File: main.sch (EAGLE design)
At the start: 50 parts, among them U1 SN65HVD10_D_8

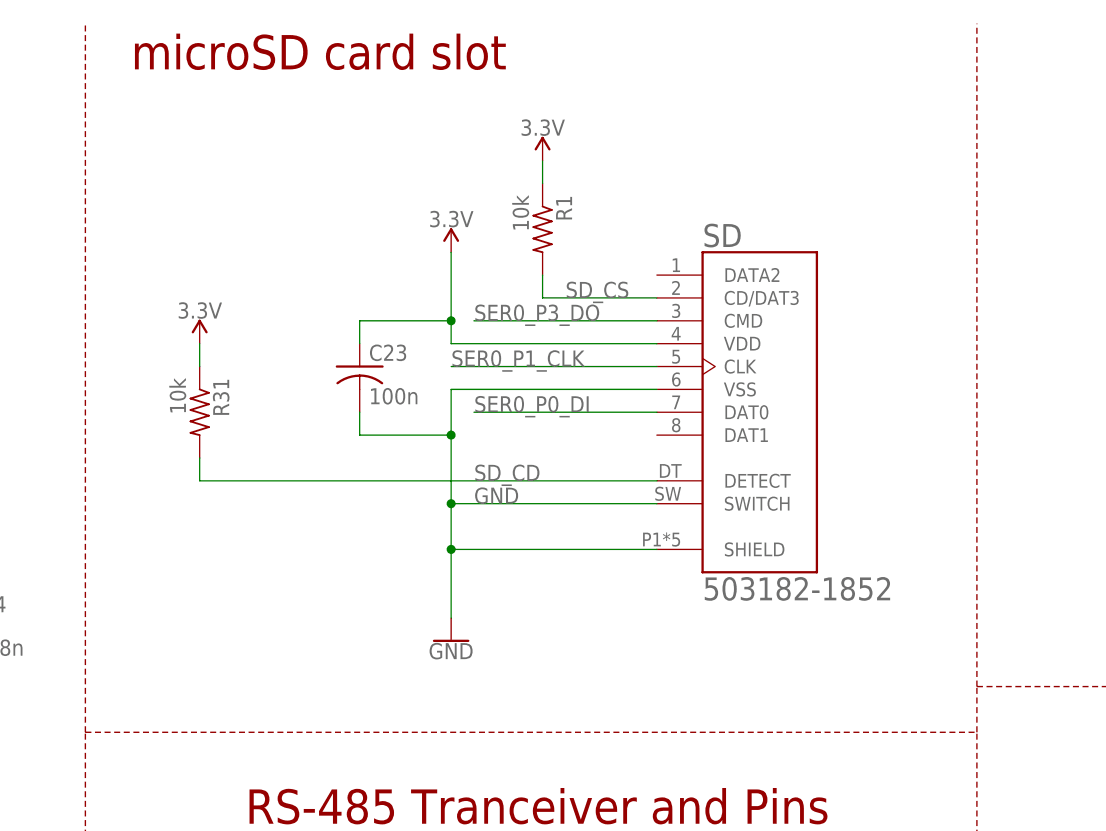
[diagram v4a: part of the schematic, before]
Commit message: Added Higned SD, rearranged silk
Added new hinged MicroSD for stability purposes, this sd card will be operating in a high g, high vibration enviornment and a spring ejection slot is not adequate. I also rearranged the labels on the silk screen as the headers were blocking a few. The SD card is also seated closer to the center, hopefully so the card no loner sticks out past the board dimensions.
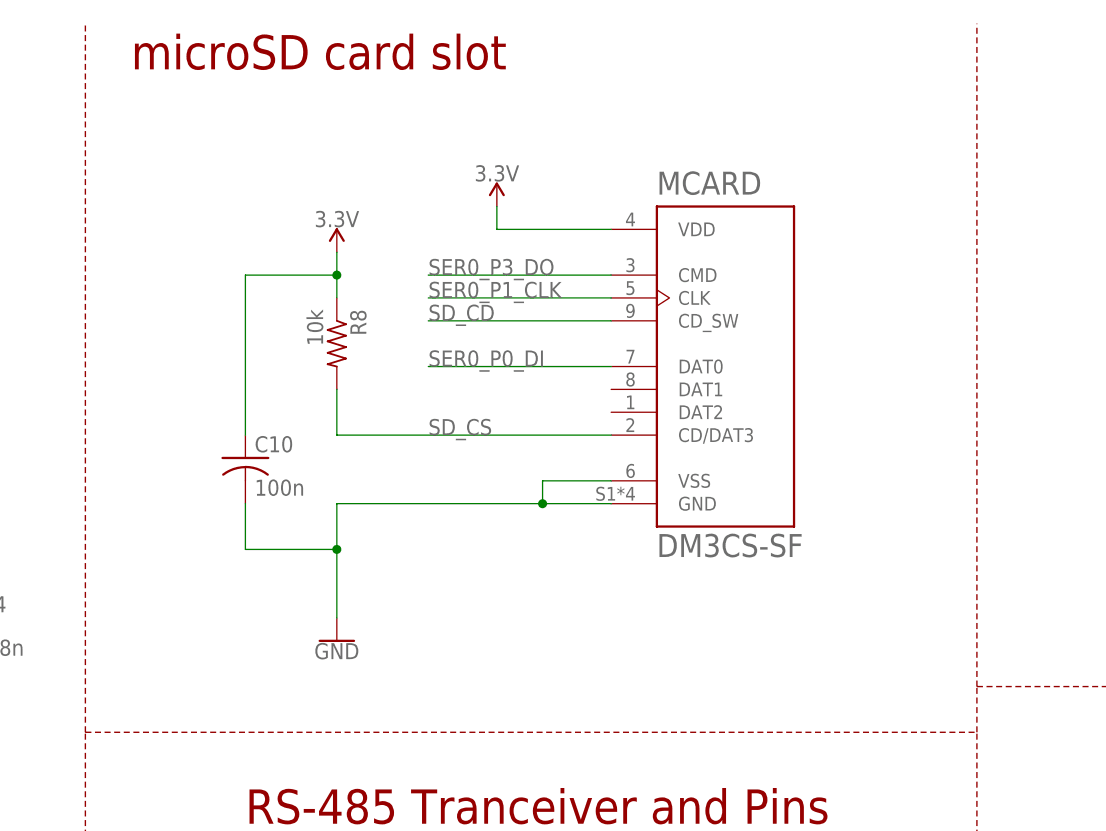
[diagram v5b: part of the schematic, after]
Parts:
- removed C23: 100n, resistor:C-USC0603
- removed R1, R31: 10k, resistor:R-US_R0603
- removed SD: 503182-1852, molex-microSD:503182-1852
- added C10: 100n, resistor:C-USC0603
- added MCARD: DM3CS-SF, DM3CS-SF:DM3CS-SF
- added R8: 10k, resistor:R-US_R0603
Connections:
- net 3.3V: now also C10.1, MCARD.VDD, R8.1; no longer C23.1, R1.1, R31.1, SD.VDD
- net GND: now also C10.2, MCARD.GND, MCARD.VSS; no longer C23.2, SD.SHIELD, SD.SWITCH, SD.VSS
- net SD_CD: now also MCARD.CD_SW; no longer R31.2, SD.DETECT
- net SD_CS: now also MCARD.CD/DAT3, R8.2; no longer R1.2, SD.CD/DAT3
- net SER0_P0_DI: now also MCARD.DAT0; no longer SD.DAT0
- net SER0_P1_CLK: now also MCARD.CLK; no longer SD.CLK
- net SER0_P3_DO: now also MCARD.CMD; no longer SD.CMD
